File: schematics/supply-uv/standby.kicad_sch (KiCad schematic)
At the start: 89 parts, among them J4 CW2B-10A-T, K1 SRD-12VDC-SL-C, Q1 5N65F, Q2 IRLML5203, Q3 IRLML5203, Q4 IRLML5203, U1 R7731, U2 EL817, U3 EL817, U4 L7805CDT-TR, U5 L7805CDT-TR, U6 TL431DBZ, U7 EL817, U8 TL432DBZ, U9 TL331, Y1 B32022A3223M000

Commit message: Board#1 schematics rewrited
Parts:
- added CLR2: HS 239-20, Library:HS-239-20, symbol My_Library:COOLER
- added D7, D8: L-2060YD, LED_THT:LED_D1.8mm_W3.3mm_H2.4mm, symbol Device:LED
- added R16, R17: 510, Resistor_SMD:R_0805_2012Metric, symbol Device:R
- added TP3: STB_GND, Library:TestPoint_Plated_Hole_D1.0mm, symbol Connector:TestPoint
- added TP4: VSYS1, TestPoint:TestPoint_Pad_2.0x2.0mm, symbol Connector:TestPoint
- added TP5: VSYS1_GND, Library:TestPoint_Plated_Hole_D1.0mm, symbol Connector:TestPoint
- added TP6: VSYS2_VCC, TestPoint:TestPoint_Pad_2.0x2.0mm, symbol Connector:TestPoint
- added TP7: VSYS2_GND, Library:TestPoint_Plated_Hole_D1.0mm, symbol Connector:TestPoint
- added TP8: +320V, TestPoint:TestPoint_Pad_2.0x2.0mm, symbol Connector:TestPoint
- U4, U5: value L7805CDT-TR -> L7805ABV; footprint (none) -> Package_TO_SOT_THT:TO-220-3_Vertical
- renumbered D8 to D10, D7 to D9, J4 to J5, R16 to R18, R17 to R19, R18 to R20, R19 to R21, R20 to R22, R21 to R23, R22 to R24, R23 to R25, R24 to R26, R25 to R27, R26 to R28, TP3 to TP9
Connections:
- net HV_GND: no longer K1.2
- net HV_VCC: now also TP8.1
- net STB_GND: now also K1.2, TP3.1
- net VSYS1_GND: now also R17.1, TP5.1
- net VSYS1_VCC: now also D8.2 (A), TP4.1
- net VSYS2_GND: now also R16.1, TP7.1
- net VSYS2_VCC: now also D7.2 (A), TP6.1
- new net: D8.1 (K), R17.2
- new net: D7.1 (K), R16.2
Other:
- note added: "17.2V, stable"
- note added: "8 ... 12 V"

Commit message: added some protection logic
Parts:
- added D2: SMBJ3.3A, Diode_SMD:D_SMB, symbol Diode:SMAJ400A
- added D8, D9: SMAJ5.0CA-TR, Diode_SMD:D_SMA, symbol Diode:ESD9B3.3ST5G
- added F3: 1.5A, Library:FuseHolder1808, symbol Device:Fuse
- added JP1: VSYS1_EN, Jumper:SolderJumper-2_P1.3mm_Open_TrianglePad1.0x1.5mm, symbol Jumper:SolderJumper_2_Open
- added JP2: VSYS2_EN, Jumper:SolderJumper-2_P1.3mm_Open_TrianglePad1.0x1.5mm, symbol Jumper:SolderJumper_2_Open
- renumbered C8 to C10, C9 to C11, C10 to C12, C11 to C13, C12 to C14, C13 to C15, C14 to C16, C15 to C17, C16 to C18, C17 to C19, C18 to C20, C19 to C21, C20 to C22, C21 to C23, C22 to C24, C23 to C25, C24 to C26, C25 to C27, C26 to C28, C27 to C29, C1 to C3, C2 to C4, C3 to C5, C4 to C6, C5 to C7, C6 to C8, C7 to C9, D8 to D10, D7 to D11, D9 to D12, D10 to D13, D2 to D3, D3 to D4, D4 to D5, D5 to D6, D6 to D7, JP1 to JP3, R18 to R16, R19 to R17, R17 to R18, R16 to R19, U9 to U10, U1 to U2, U2 to U3, U3 to U4, U4 to U5, U5 to U6, U6 to U7, U7 to U8, U8 to U9
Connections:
- net HV_GND: now also D2.2 (A2)
- net HV_VCC: now also F3.1; no longer C7.2, R2.2, R8.2, TR1.13
- net VSYS1_GND: now also D9.1 (A1)
- net VSYS1_VCC: now also JP1.2 (B); no longer C19.1, C22.1, D10.2 (A), L1.2
- net VSYS2_GND: now also D8.1 (A1)
- net VSYS2_VCC: now also JP2.2 (B); no longer C20.1, C23.1, D11.2 (A), L2.2
- net at C6.2, R10.2, U2.4 (CS): now also D2.1 (A1)
- new net: C19.1, C22.1, D10.2 (A), D9.2 (A2), JP1.1 (A), L1.2
- new net: C20.1, C23.1, D11.2 (A), D8.2 (A2), JP2.1 (A), L2.2
- new net HV_VCC_FUSE: C7.2, F3.2, R2.2, R8.2, TR1.13
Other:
- note added: "1.1A"
- moved on the sheet: C6, D10, D11, D12, R18, R19, R22

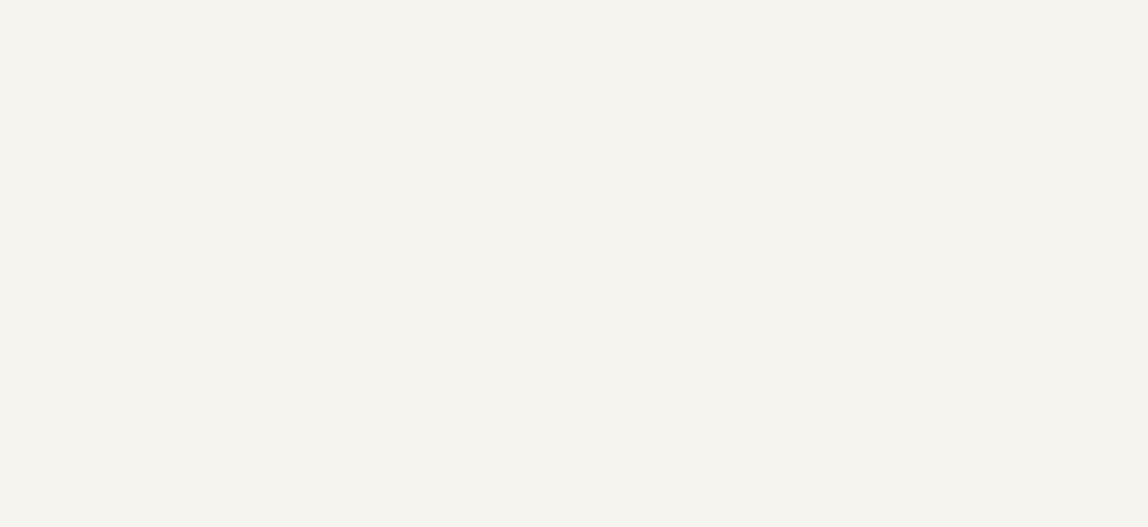
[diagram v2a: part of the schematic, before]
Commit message: changed operation amplifier
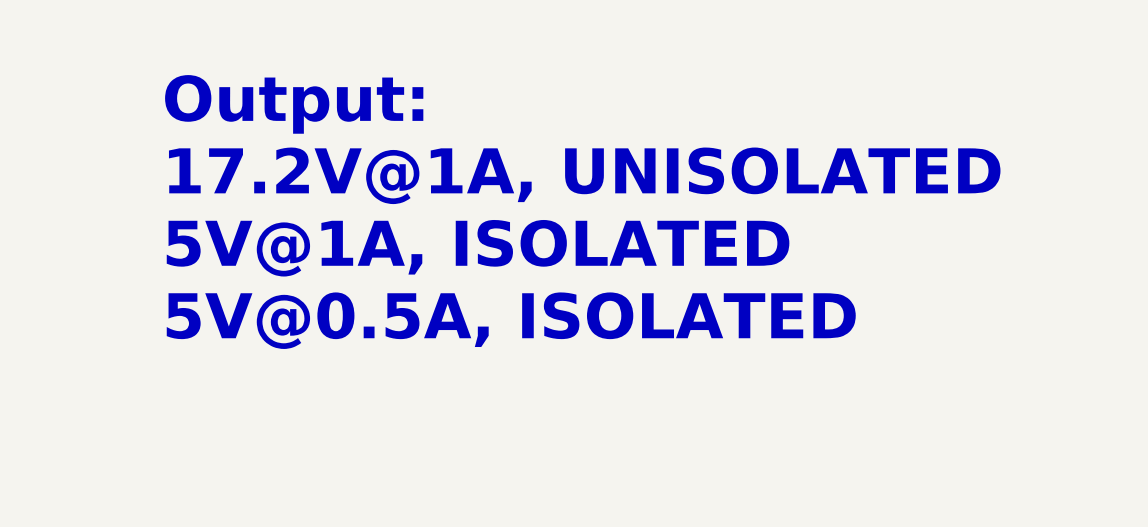
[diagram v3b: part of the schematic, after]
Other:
- note added: "Output: 17.2V@1A, UNISOLATED 5V@1A, ISOLATED 5V@0.5A, ISOLATED"
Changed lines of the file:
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@@
+		)
+	)
+	(text "Output:\n17.2V@1A, UNISOLATED\n5V@1A, ISOLATED\n5V@0.5A, ISOLATED\n\n"
+		(exclude_from_sim no)
+		(at 491.744 62.23 0)
+		(effects
+			(font
+				(size 5 5)
+				(bold yes)
+			)
+			(justify left bottom)
 		)
 	)

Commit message: start board#1 tracing
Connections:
- net HV_VCC: no longer C3.1, C4.2
- net HV_VCC_FUSE: now also C3.1, C4.2
- net STARTUP_PROTECT_OUT: now also D1.2; no longer D1.3
- net STB_GND: now also TR1.14; no longer TR1.3
- net VSYS1_GND: now also TR1.6; no longer TR1.2
- net VSYS2_GND: now also TR1.2; no longer TR1.8
- net at D6.2 (A): now also TR1.8; no longer TR1.4
- net at D5.2 (A): now also TR1.12; no longer TR1.5
- net at D7.2 (A): now also TR1.4; no longer TR1.6
- net at R13.2: now also TR1.5; no longer TR1.9
- net at J5.1 (Pin_1), RV1.1: now also D1.3; no longer D1.2
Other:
- moved on the sheet: D1
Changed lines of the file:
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@@
 	(wire
 		(pts
+			(xy 111.76 50.8) (xy 113.03 50.8)
+		)
+		(stroke
+			(width 0)
+			(type default)
+		)
+	)
+	(wire
+		(pts
 			(xy 134.62 318.77) (xy 134.62 311.15)
 		)
@@
 	(wire
 		(pts
-			(xy 95.25 50.8) (xy 96.52 50.8)
-		)
-		(stroke
-			(width 0)
-			(type default)
-		)
-	)
-	(wire
-		(pts
 			(xy 210.82 318.77) (xy 232.41 318.77)
 		)
@@
 	(wire
 		(pts
-			(xy 111.76 39.37) (xy 74.93 39.37)
+			(xy 113.03 39.37) (xy 74.93 39.37)
 		)
 		(stroke
@@
 	(wire
 		(pts
-			(xy 111.76 50.8) (xy 111.76 39.37)
+			(xy 113.03 50.8) (xy 113.03 39.37)
 		)
 		(stroke
@@
 	(wire
 		(pts
+			(xy 95.25 50.8) (xy 96.52 50.8)
+		)
+		(stroke
+			(width 0)
+			(type default)
+		)
+	)
+	(wire
+		(pts
 			(xy 261.62 128.27) (xy 261.62 166.37)
 		)
@@
 		)
 	)
+	(label "HV_VCC_FUSE"
+		(at 72.39 91.44 180)
+		(fields_autoplaced yes)
+		(effects
+			(font
+				(size 1.27 1.27)
+			)
+			(justify right bottom)
+		)
+	)
 	(label "FEEDBACK"
 		(at 78.74 176.53 180)
@@
 		)
 	)
-	(hierarchical_label "HV_VCC"
-		(shape input)
-		(at 72.39 91.44 180)
-		(fields_autoplaced yes)
-		(effects
-			(font
-				(size 1.27 1.27)
-			)
-			(justify right)
-		)
-	)
 	(hierarchical_label "VSYS2_VCC"
 		(shape input)
@@
 		(pin "13"
 		)
-		(pin "3"
+		(pin "6"
 		)
 		(pin "5"
@@
 		(pin "7"
 		)
-		(pin "9"
+		(pin "12"
 		)
 		(pin "4"
@@
 		(pin "2"
 		)
-		(pin "6"
+		(pin "14"
 		)
 		(instances
@@
 	(symbol
 		(lib_id "Diode_Bridge:KBU8M")
-		(at 104.14 50.8 90)
+		(at 104.14 50.8 270)
+		(mirror x)
 		(unit 1)
 		(exclude_from_sim no)
@@
 		(dnp no)
 		(property "Reference" "D1"
-			(at 111.76 54.61 90)
+			(at 96.52 54.61 90)
 			(effects
 				(font
@@
 		)
 		(property "Value" "KBU1010"
-			(at 111.76 57.15 90)
+			(at 96.52 57.15 90)
 			(effects
 				(font
@@
 		)
 		(property "Footprint" "Diode_THT:Diode_Bridge_Vishay_KBU"
-			(at 100.965 46.99 0)
+			(at 107.315 46.99 0)
 			(effects
 				(font

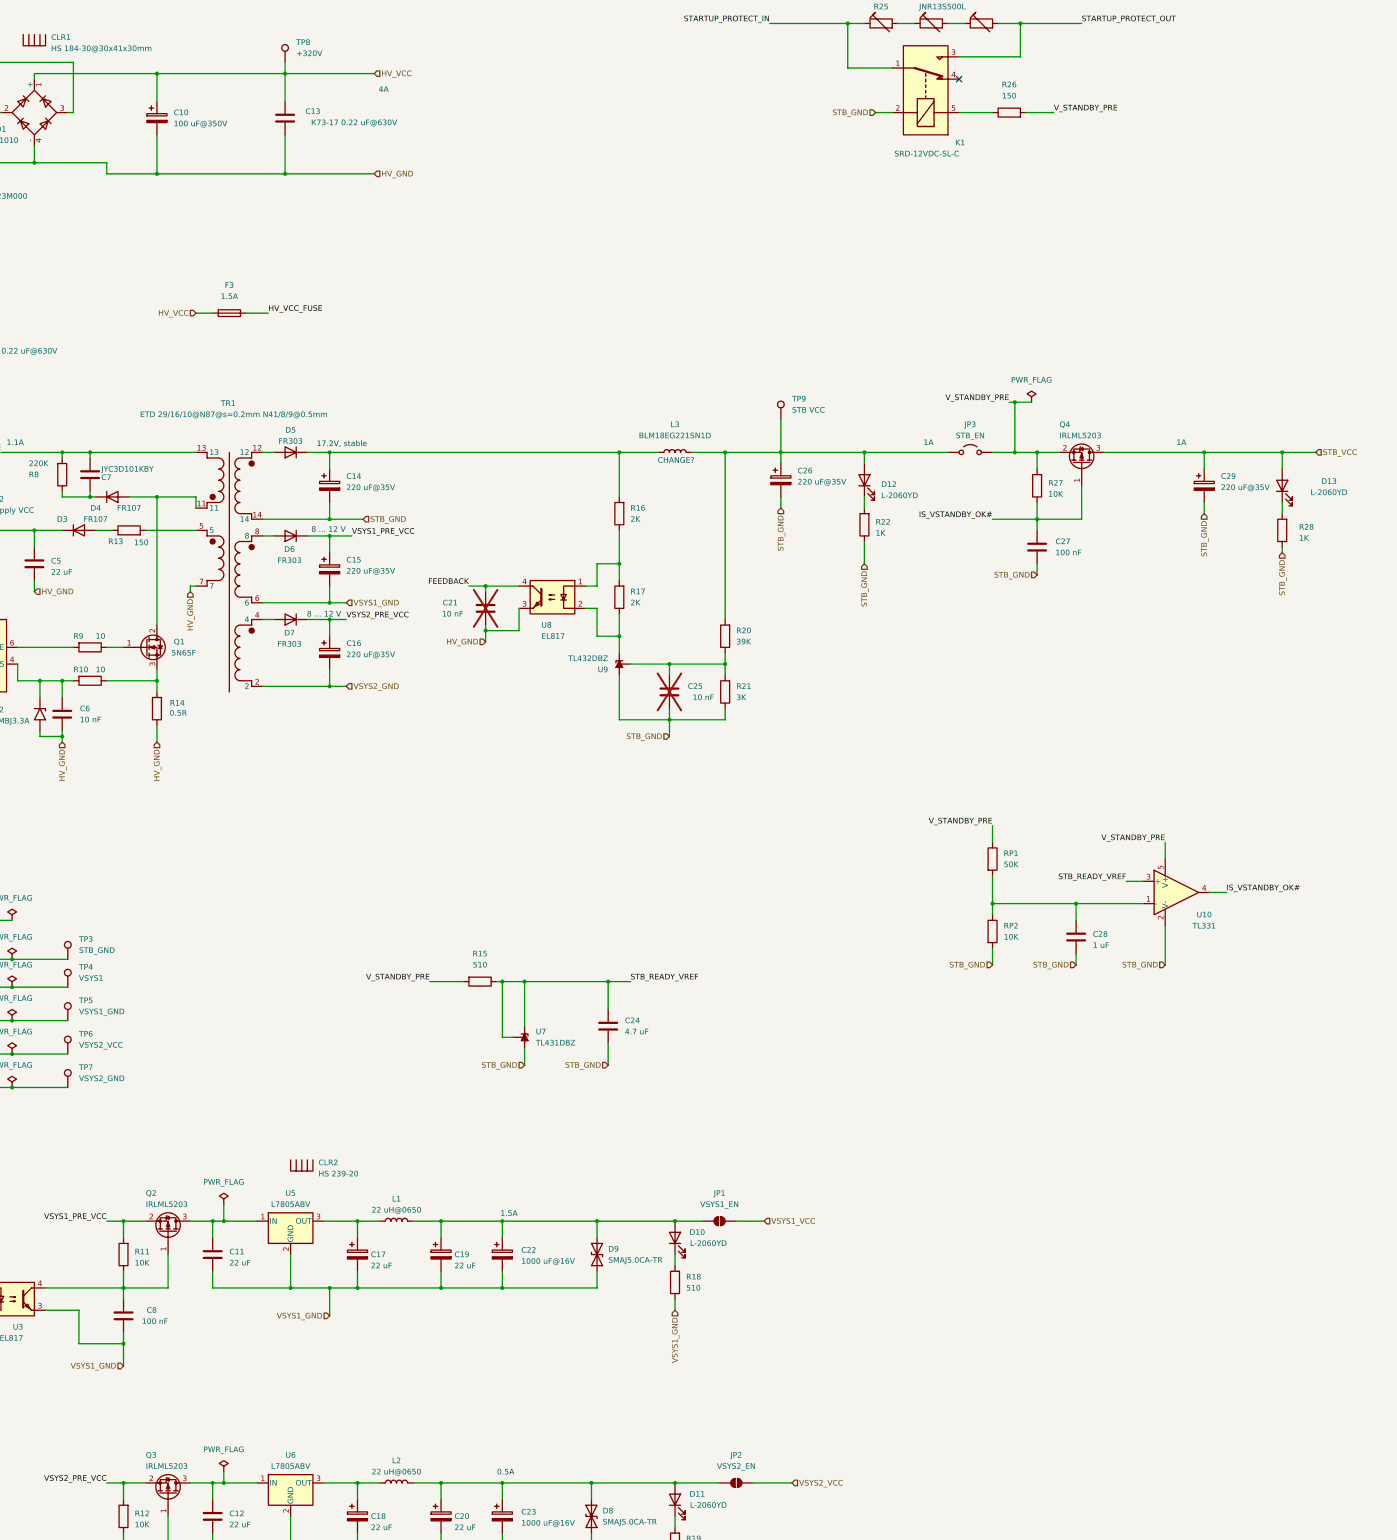
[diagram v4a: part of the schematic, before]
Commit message: First board routing completed. I will review it few days later and maybe optimize something, but base worki done
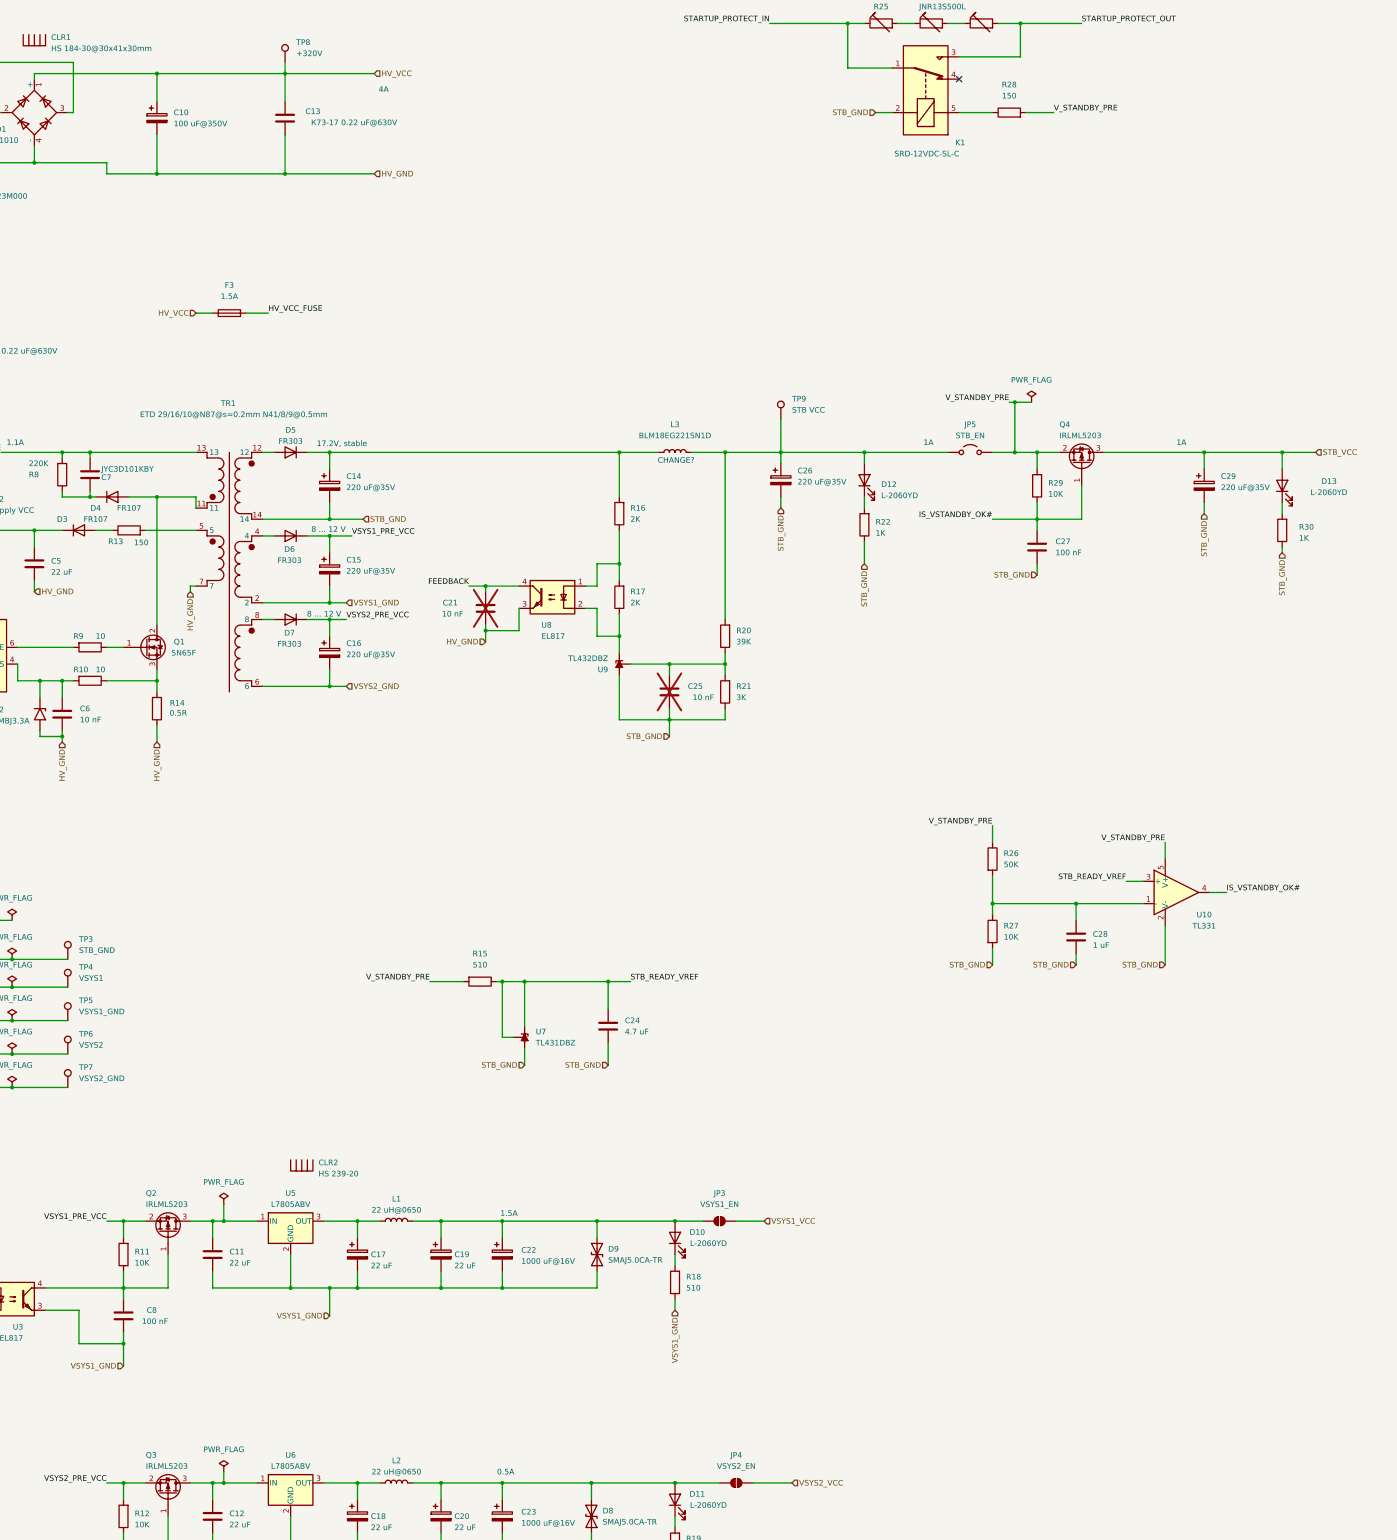
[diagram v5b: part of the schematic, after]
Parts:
- TP6: value VSYS2_VCC -> VSYS2
- TP9: footprint TestPoint:TestPoint_Pad_2.0x2.0mm -> TestPoint:TestPoint_Pad_1.0x1.0mm
- renumbered JP1 to JP3, JP2 to JP4, JP3 to JP5, RP1 to R26, RP2 to R27, R26 to R28, R27 to R29, R28 to R30
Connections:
- net VSYS1_GND: now also TR1.2; no longer TR1.6
- net VSYS2_GND: now also TR1.6; no longer TR1.2
- net at D6.2 (A): now also TR1.4; no longer TR1.8
- net at D7.2 (A): now also TR1.8; no longer TR1.4
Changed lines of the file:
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@@
 		(dnp no)
 		(fields_autoplaced yes)
-		(property "Reference" "JP3"
+		(property "Reference" "JP5"
 			(at 317.5 121.92 0)
 			(effects
@@
 			(project "supply-uv"
 				(path "/ef40850c-d0bf-4cba-961b-9aba418f8e73/14317b0a-1f8a-4d8b-b159-cbc20c410ffd"
-					(reference "JP3")
+					(reference "JP5")
 					(unit 1)
 				)
@@
 		(dnp no)
 		(fields_autoplaced yes)
-		(property "Reference" "R27"
+		(property "Reference" "R29"
 			(at 335.28 135.255 0)
 			(effects
@@
 			(project "supply-uv"
 				(path "/ef40850c-d0bf-4cba-961b-9aba418f8e73/14317b0a-1f8a-4d8b-b159-cbc20c410ffd"
-					(reference "R27")
+					(reference "R29")
 					(unit 1)
 				)
@@
 		(dnp no)
 		(fields_autoplaced yes)
-		(property "Reference" "RP1"
+		(property "Reference" "R26"
 			(at 325.12 219.7099 0)
 			(effects
@@
 			(project "supply-uv"
 				(path "/ef40850c-d0bf-4cba-961b-9aba418f8e73/14317b0a-1f8a-4d8b-b159-cbc20c410ffd"
-					(reference "RP1")
+					(reference "R26")
 					(unit 1)
 				)
@@
 		(dnp no)
 		(fields_autoplaced yes)
-		(property "Reference" "R26"
+		(property "Reference" "R28"
 			(at 326.39 44.45 90)
 			(effects
@@
 			(project "supply-uv"
 				(path "/ef40850c-d0bf-4cba-961b-9aba418f8e73/14317b0a-1f8a-4d8b-b159-cbc20c410ffd"
-					(reference "R26")
+					(reference "R28")
 					(unit 1)
 				)
@@
 			)
 		)
-		(property "Footprint" "TestPoint:TestPoint_Pad_2.0x2.0mm"
+		(property "Footprint" "TestPoint:TestPoint_Pad_1.0x1.0mm"
 			(at 279.4 120.65 0)
 			(effects
@@
 		(dnp no)
 		(fields_autoplaced yes)
-		(property "Reference" "RP2"
+		(property "Reference" "R27"
 			(at 325.12 236.2199 0)
 			(effects
@@
 			(project "supply-uv"
 				(path "/ef40850c-d0bf-4cba-961b-9aba418f8e73/14317b0a-1f8a-4d8b-b159-cbc20c410ffd"
-					(reference "RP2")
+					(reference "R27")
 					(unit 1)
 				)
@@
 		(dnp no)
 		(fields_autoplaced yes)
-		(property "Reference" "JP2"
+		(property "Reference" "JP4"
 			(at 264.16 356.87 0)
 			(effects
@@
 			(project "supply-uv"
 				(path "/ef40850c-d0bf-4cba-961b-9aba418f8e73/14317b0a-1f8a-4d8b-b159-cbc20c410ffd"
-					(reference "JP2")
+					(reference "JP4")
 					(unit 1)
 				)
@@
 		(dnp no)
 		(fields_autoplaced yes)
-		(property "Reference" "JP1"
+		(property "Reference" "JP3"
 			(at 260.35 297.18 0)
 			(effects
@@
 			(project ""
 				(path "/ef40850c-d0bf-4cba-961b-9aba418f8e73/14317b0a-1f8a-4d8b-b159-cbc20c410ffd"
-					(reference "JP1")
+					(reference "JP3")
 					(unit 1)
 				)
@@
 		(on_board yes)
 		(dnp no)
-		(property "Reference" "R28"
+		(property "Reference" "R30"
 			(at 392.43 145.288 0)
 			(effects
@@
 			(project "supply-uv"
 				(path "/ef40850c-d0bf-4cba-961b-9aba418f8e73/14317b0a-1f8a-4d8b-b159-cbc20c410ffd"
-					(reference "R28")
+					(reference "R30")
 					(unit 1)
 				)
@@
 			)
 		)
-		(property "Value" "VSYS2_VCC"
+		(property "Value" "VSYS2"
 			(at 114.3 263.3979 0)
 			(effects
